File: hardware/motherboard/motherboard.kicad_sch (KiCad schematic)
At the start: 20 parts, among them J1 Custom_PCIe_x4, J10 Conn_01x50_MountingPin, J11 Conn_01x50_MountingPin, J12 Barrel_Jack_Switch_Pin3Ring, J2 Custom_PCIe_x4, J3 Custom_PCIe_x4, J4 Custom_PCIe_x4, J5 Custom_PCIe_x4, J6 Custom_PCIe_x4, J7 Custom_PCIe_x4, J8 Custom_PCIe_x4, J9 Conn_01x50_MountingPin, U1 74HC138, U3 SN74LV595, U5 74HC138

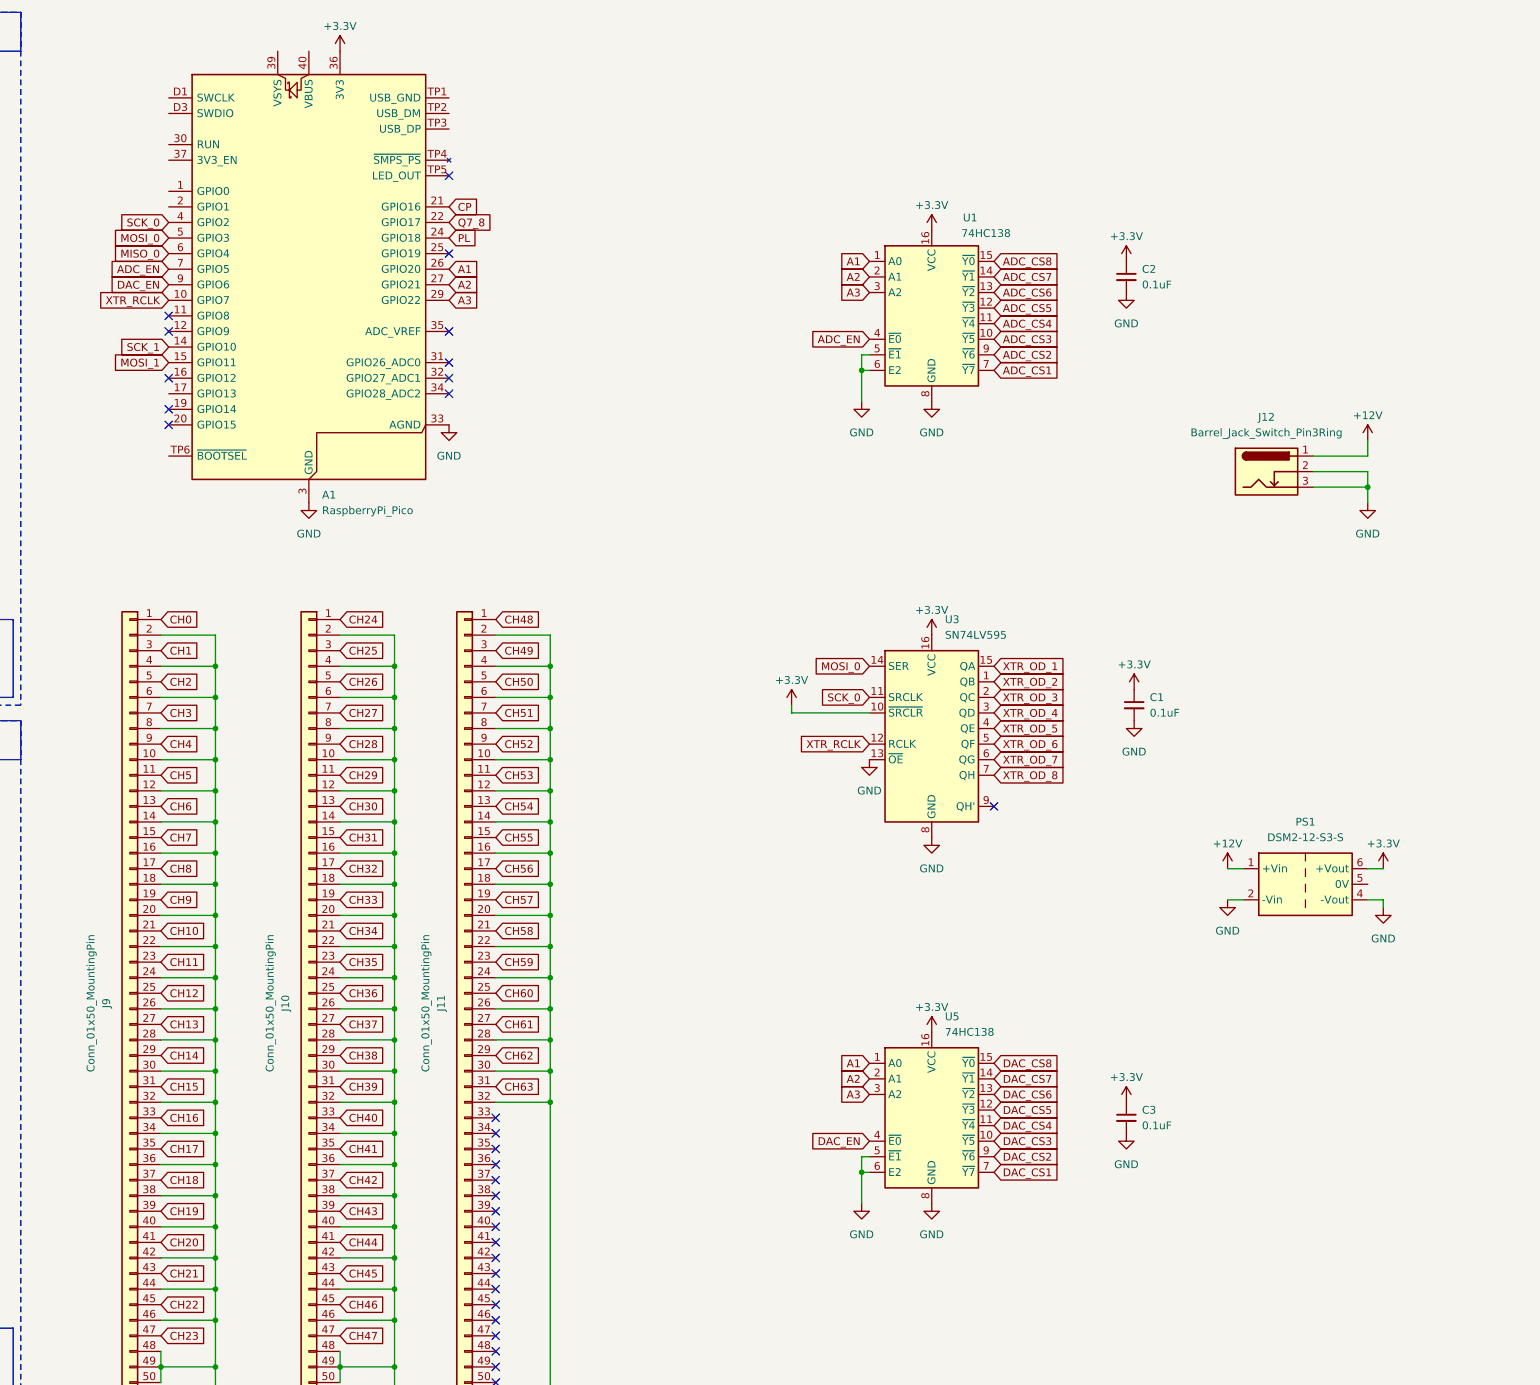
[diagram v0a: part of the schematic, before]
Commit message: updated daughterboard with eeprom and some layout improvements and padne simulations
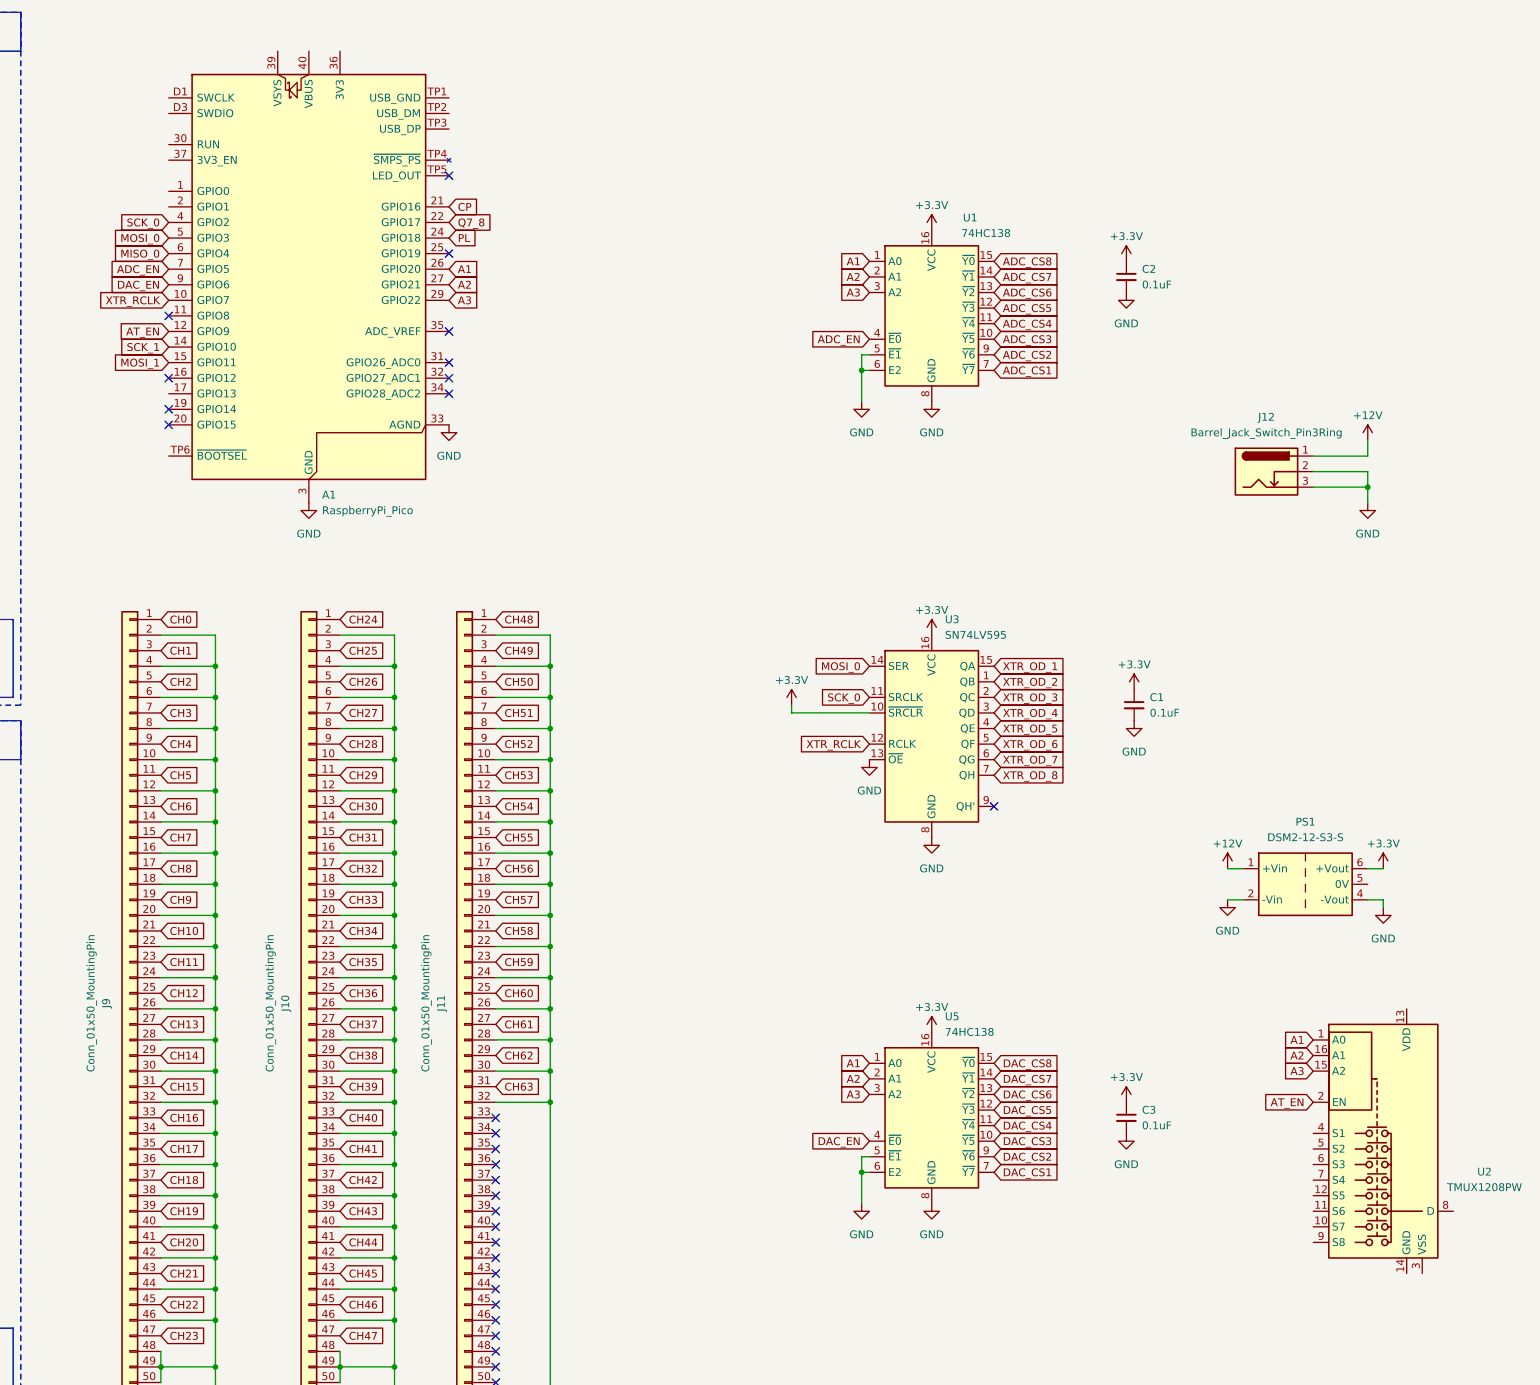
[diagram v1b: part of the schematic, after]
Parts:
- added U2: TMUX1208PW, Package_SO:TSSOP-16_4.4x5mm_P0.65mm, symbol Analog_Switch:TMUX1208PW
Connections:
- net +3.3V: no longer A1.36 (3V3)
- net A1: now also U2.1 (A0)
- net A2: now also U2.16 (A1)
- net A3: now also U2.15 (A2)
- net AT_EN: now reaches A1.12 (GPIO9)
- net AT_EN: now also U2.2 (EN)
- no-connect marks 46 -> 45

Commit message: update pcb
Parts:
- added C4: 0.1uF, Capacitor_SMD:C_0603_1608Metric, symbol Device:C_Small
- added TP1, TP2, TP3, TP4: TestPoint, Connector_PinHeader_2.54mm:PinHeader_1x01_P2.54mm_Vertical, symbol Connector:TestPoint
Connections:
- net +12V: now also J1.A30 (+12V), J2.A30 (+12V), J3.A30 (+12V), J4.A30 (+12V), J5.A30 (+12V), J6.A30 (+12V), J7.A30 (+12V), J8.A30 (+12V); no longer J1.A3 (+3.3V), J2.A3 (+3.3V), J3.A3 (+3.3V), J4.A3 (+3.3V), J5.A3 (+3.3V), J6.A3 (+3.3V), J7.A3 (+3.3V), J8.A3 (+3.3V)
- net +3.3V: now also U2.13 (VDD), C4.1; no longer J1.B9 (MISO_1), J2.B9 (MISO_1), J3.B9 (MISO_1), J4.B9 (MISO_1), J5.B9 (MISO_1), J6.B9 (MISO_1), J7.B9 (MISO_1), J8.B9 (MISO_1)
- net GND: now also J1.A3 (GND), J2.A3 (GND), J3.A3 (GND), J4.A3 (GND), J5.A3 (GND), J6.A3 (GND), J7.A3 (GND), J8.A3 (GND), U2.14 (GND), U2.3 (VSS), C4.2; no longer J1.A7 (GND), J2.A7 (GND), J3.A7 (GND), J4.A7 (GND), J5.A7 (GND), J6.A7 (GND), J7.A7 (GND), J8.A7 (GND)
- net MISO_0: now also TP3.1
- net MOSI_0: now also TP2.1
- net SCK_0: now also TP1.1
- net MISO_1: now reaches A1.16 (GPIO12)
- net MISO_1: now also J1.B9 (MISO_1), J2.B9 (MISO_1), J3.B9 (MISO_1), J4.B9 (MISO_1), J5.B9 (MISO_1), J6.B9 (MISO_1), J7.B9 (MISO_1), J8.B9 (MISO_1)
- net AT_MUX: now reaches A1.17 (GPIO13)
- net AT_MUX: now also U2.8 (D)
- net AT7: now reaches U2.10 (S7)
- net AT7: now also J7.A7 (AT)
- net AT6: now reaches U2.11 (S6)
- net AT6: now also J6.A7 (AT)
- net AT5: now reaches U2.12 (S5)
- net AT5: now also J5.A7 (AT)
- net AT1: now reaches U2.4 (S1)
- net AT1: now also J1.A7 (AT)
- net AT2: now reaches U2.5 (S2)
- net AT2: now also J2.A7 (AT)
- net AT3: now reaches U2.6 (S3)
- net AT3: now also J3.A7 (AT)
- net AT4: now reaches U2.7 (S4)
- net AT4: now also J4.A7 (AT)
- net AT8: now reaches U2.9 (S8)
- net AT8: now also J8.A7 (AT)
- no-connect marks 45 -> 36
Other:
- moved on the sheet: C3, J12, PS1, U5
